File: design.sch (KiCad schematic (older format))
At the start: 30 parts

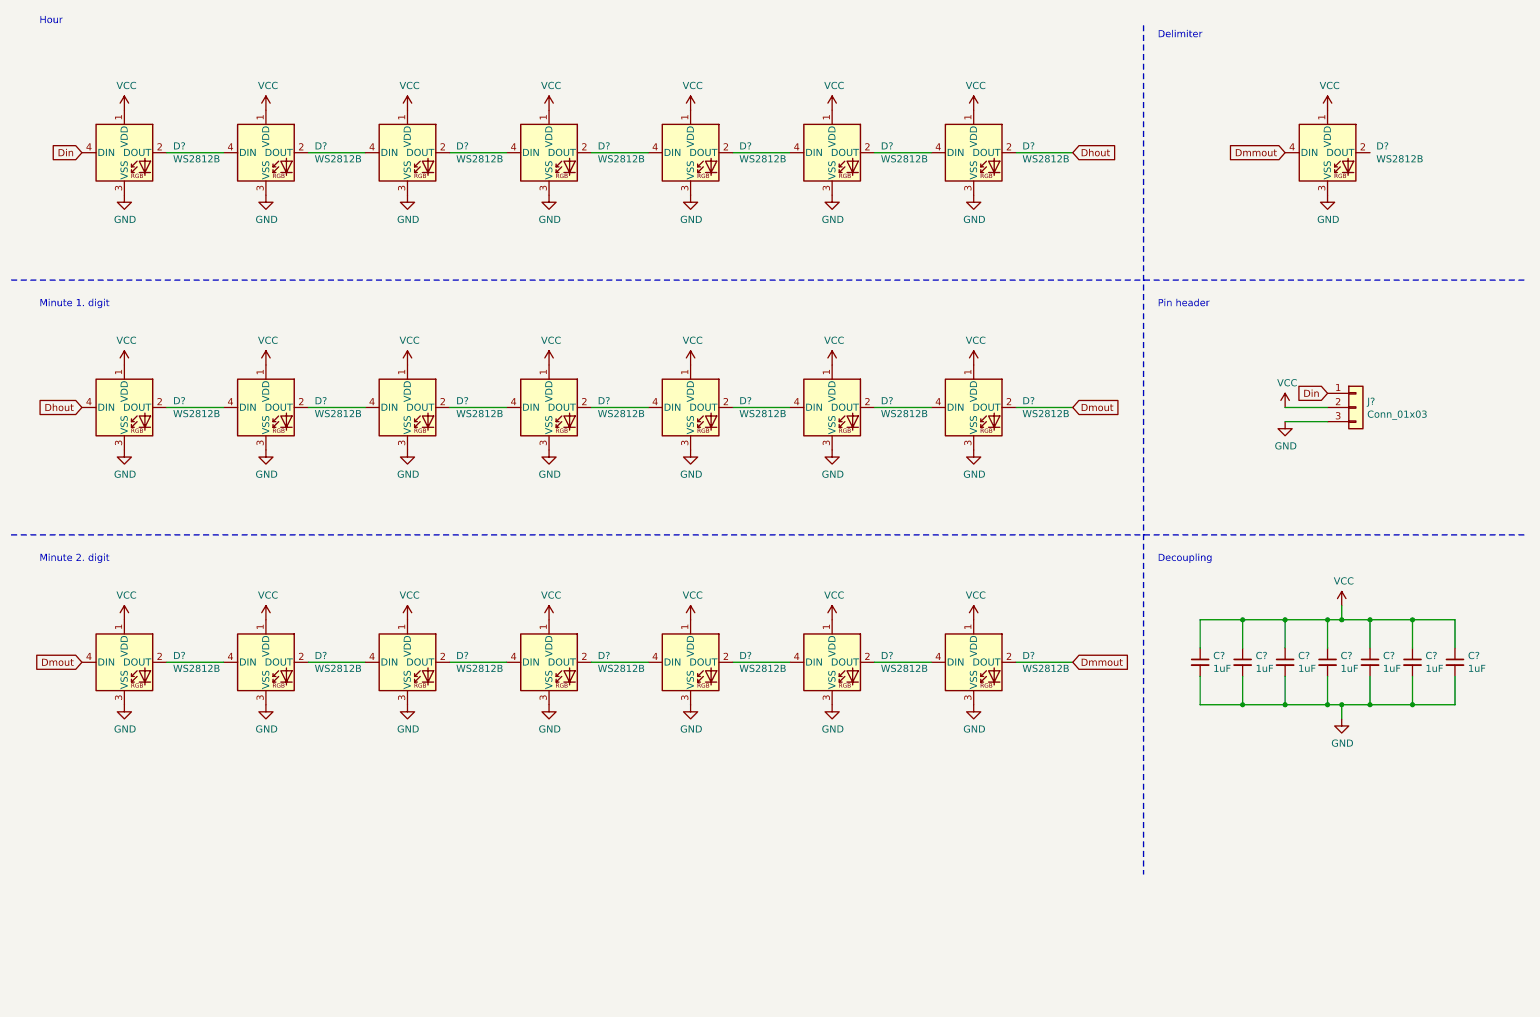
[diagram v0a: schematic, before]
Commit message: PCB: placed components
and some cosmetic SCH stuff
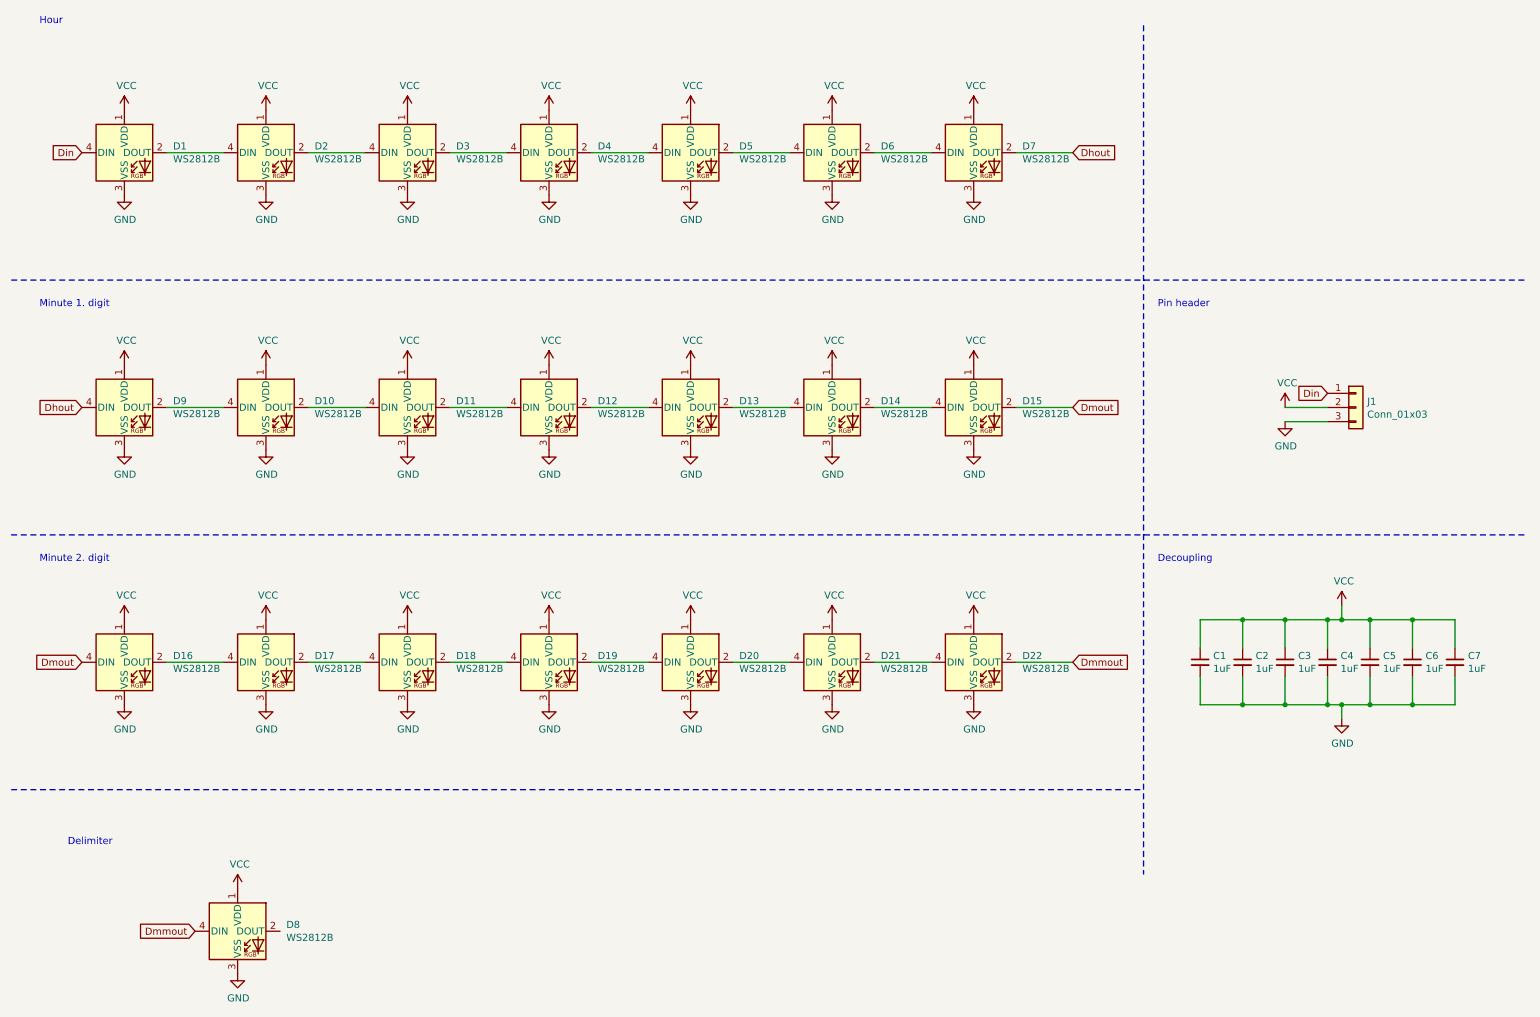
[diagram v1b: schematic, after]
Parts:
- C1, C2, C3, C4, C5, C6, C7: renamed from C?; footprint (none) -> Capacitor_SMD:C_0805_2012Metric
- gave numbers to parts that had none: 23
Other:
- moved on the sheet: D8

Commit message: SCH: annotation in the segment order
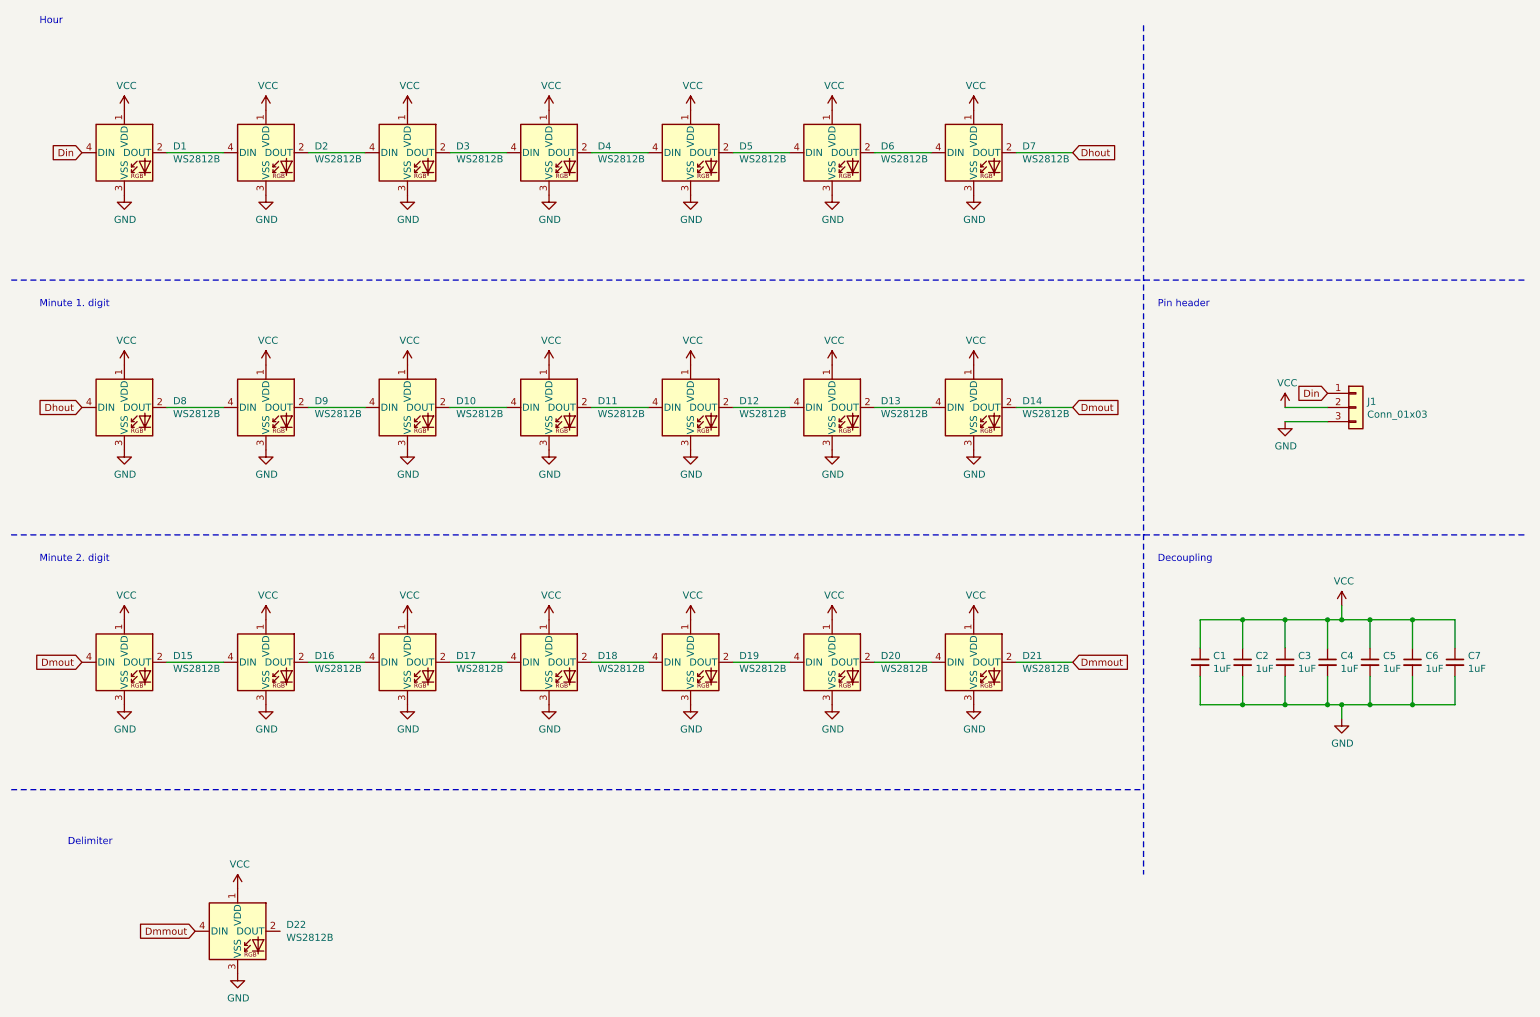
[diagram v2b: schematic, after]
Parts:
- renumbered D11 to D10, D12 to D11, D13 to D12, D14 to D13, D15 to D14, D16 to D15, D17 to D16, D18 to D17, D19 to D18, D20 to D19, D21 to D20, D22 to D21, D8 to D22, D9 to D8, D10 to D9

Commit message: add pinheader footprint
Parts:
- J1: footprint (none) -> Connector_PinHeader_2.54mm:PinHeader_1x03_P2.54mm_Vertical_SMD_Pin1Left
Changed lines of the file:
@@
 F 0 "J1" H 10080 3342 50  0000 L CNN
 F 1 "Conn_01x03" H 10080 3251 50  0000 L CNN
-F 2 "" H 10000 3300 50  0001 C CNN
+F 2 "Connector_PinHeader_2.54mm:PinHeader_1x03_P2.54mm_Vertical_SMD_Pin1Left" H 10000 3300 50  0001 C CNN
 F 3 "~" H 10000 3300 50  0001 C CNN
 	1    10000 3300
